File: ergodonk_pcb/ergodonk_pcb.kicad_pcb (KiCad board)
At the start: 2 copper layers, 184 x 152.6 mm, 120 parts, among them J1 AudioJack4, Q1 TIP120, SW1 SW_PUSH-MX_W_LED, SW4 SW_PUSH

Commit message: Button & LED reference sync
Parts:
- removed SW1: SW_PUSH-MX_W_LED, SofleChoc:SK6812MINI_and_cherry
- removed SW4: SW_PUSH, SofleChoc:Choc_Hotswap_SK6812MiniE

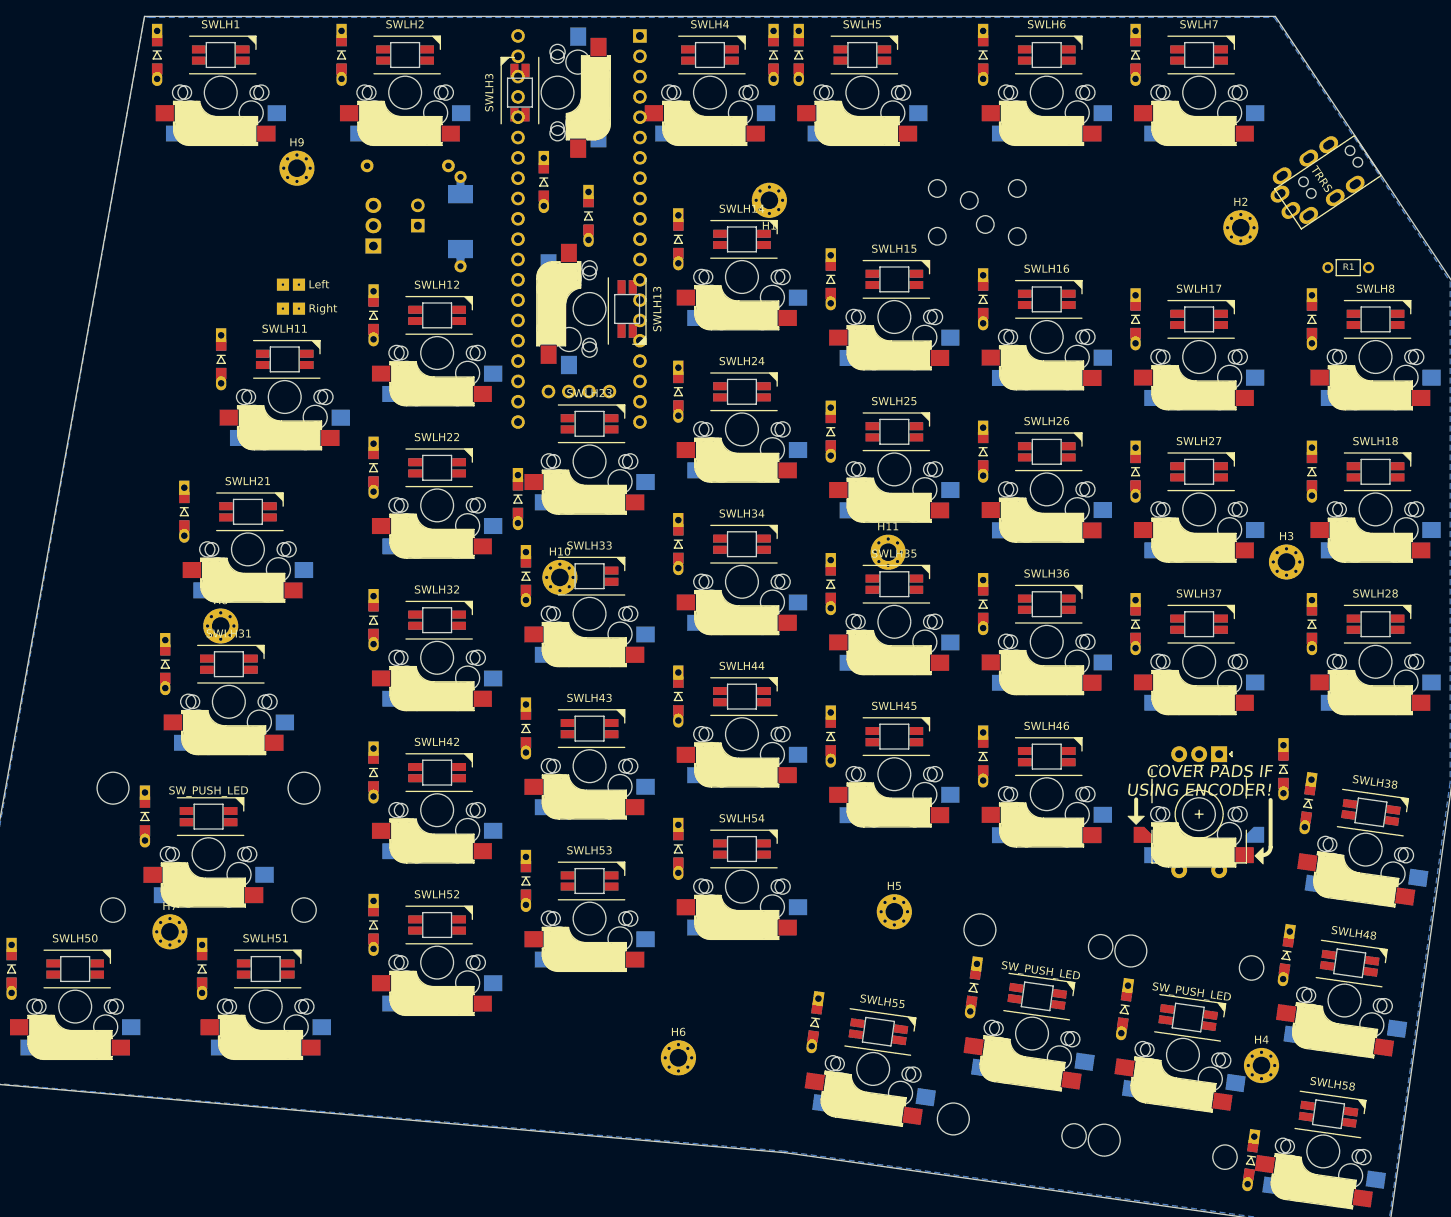
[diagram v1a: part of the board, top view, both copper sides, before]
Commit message: Reveresed nrow/column umbering systme to support double sided
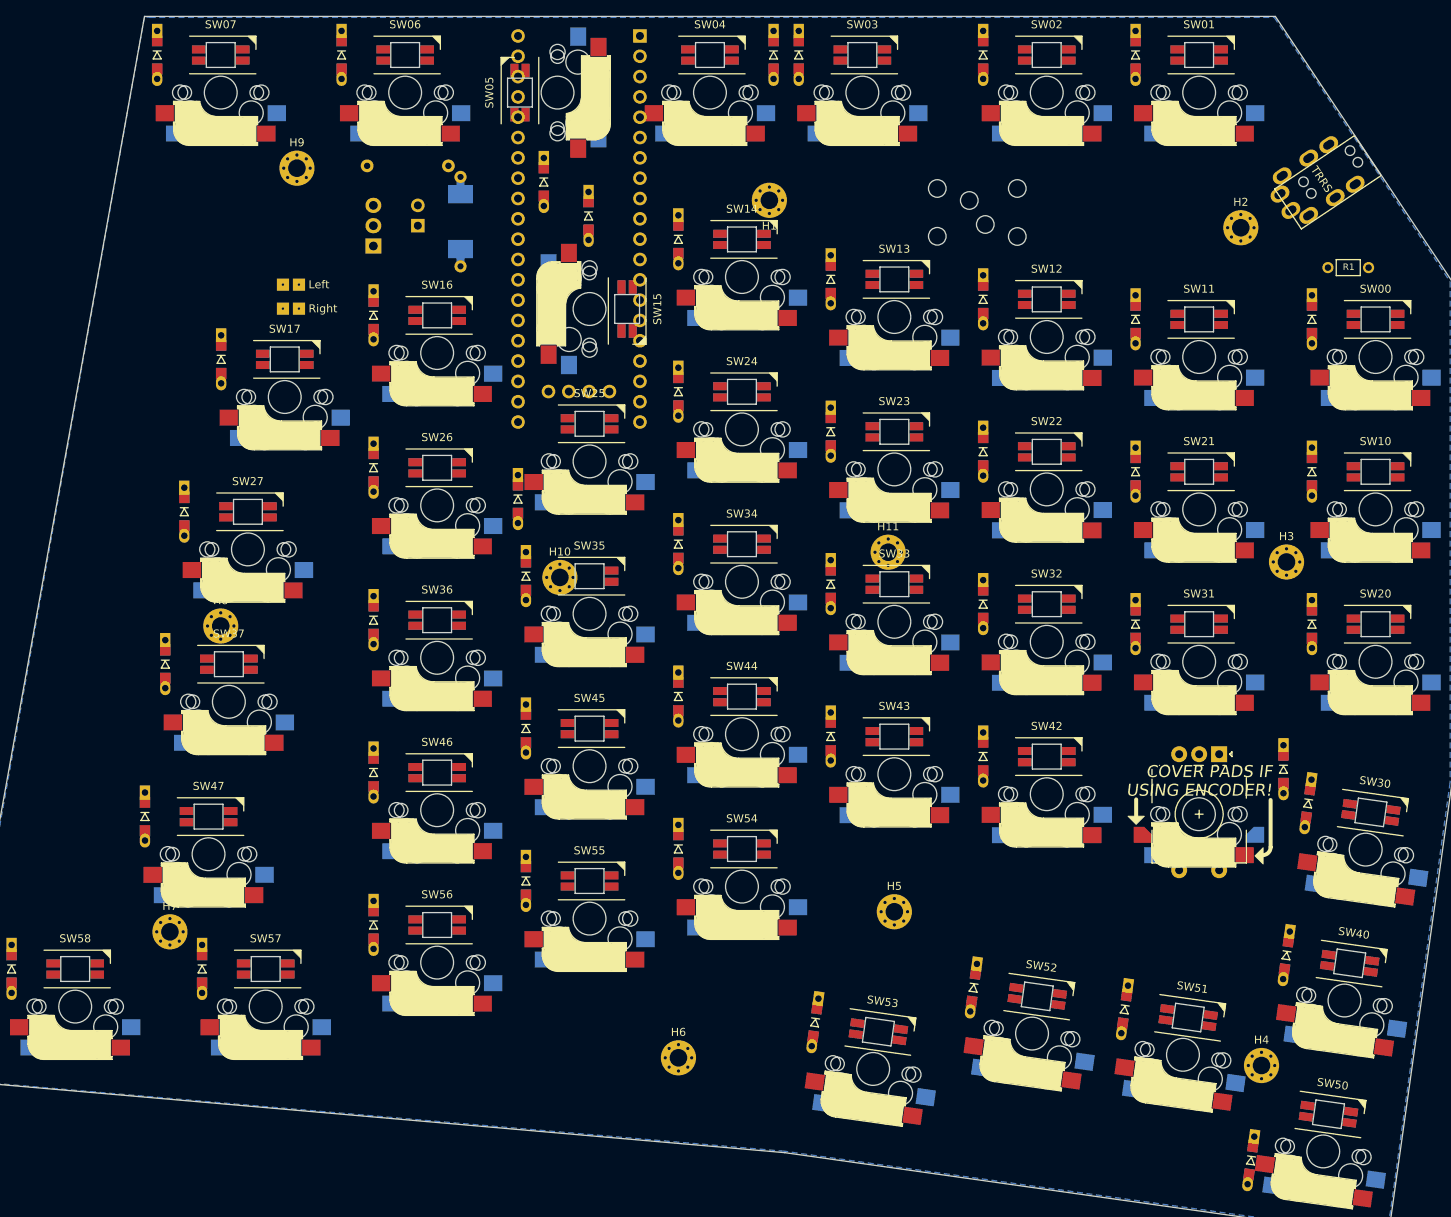
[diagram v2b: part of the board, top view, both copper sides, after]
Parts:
- SW27: renamed from SWLH21; footprint ergodonk_kicad_library:CherryMX_DoubleSided_Hotswap_miniE_1.5u -> ergodonk_kicad_library:CherryMX_DoubleSided_Hotswap_miniE
- SW37: renamed from SWLH31; footprint ergodonk_kicad_library:CherryMX_DoubleSided_Hotswap_miniE_1.75u -> ergodonk_kicad_library:CherryMX_DoubleSided_Hotswap_miniE
- SW47: renamed from SWLH41; footprint ergodonk_kicad_library:CherryMX_DoubleSided_Hotswap_miniE_2u -> ergodonk_kicad_library:CherryMX_DoubleSided_Hotswap_miniE
- SW51: renamed from SWLH57; footprint ergodonk_kicad_library:CherryMX_DoubleSided_Hotswap_miniE_2u_Vertical -> ergodonk_kicad_library:CherryMX_DoubleSided_Hotswap_miniE
- SW52: renamed from SWLH56; footprint ergodonk_kicad_library:CherryMX_DoubleSided_Hotswap_miniE_2u_Vertical -> ergodonk_kicad_library:CherryMX_DoubleSided_Hotswap_miniE
- SW53: renamed from SWLH55; footprint ergodonk_kicad_library:CherryMX_DoubleSided_Hotswap_miniE_1.25u_Vertical -> ergodonk_kicad_library:CherryMX_DoubleSided_Hotswap_miniE
- SW57: renamed from SWLH51; footprint ergodonk_kicad_library:CherryMX_DoubleSided_Hotswap_miniE_1.25u -> ergodonk_kicad_library:CherryMX_DoubleSided_Hotswap_miniE
- SW58: renamed from SWLH50; footprint ergodonk_kicad_library:CherryMX_DoubleSided_Hotswap_miniE_1.25u -> ergodonk_kicad_library:CherryMX_DoubleSided_Hotswap_miniE
- renumbered D8 to D00, D7 to D01, D6 to D02, D5 to D03, D4 to D04, D3 to D05, D2 to D06, D1 to D07, D18 to D10, D17 to D11, D16 to D12, D15 to D13, D13 to D15, D12 to D16, D11 to D17, D28 to D20, D27 to D21, D26 to D22, D25 to D23, D23 to D25, D22 to D26, D21 to D27, D38 to D30, D37 to D31, D36 to D32, D35 to D33, D33 to D35, D32 to D36, D31 to D37, D48 to D40, D47 to D41, D46 to D42, D45 to D43, D43 to D45, D42 to D46, D41 to D47, D58 to D50, D57 to D51, D56 to D52, D55 to D53, D53 to D55, D52 to D56, D51 to D57, D50 to D58, SWLH8 to SW00, SWLH7 to SW01, SWLH6 to SW02, SWLH5 to SW03, SWLH4 to SW04, SWLH3 to SW05, SWLH2 to SW06, SWLH1 to SW07, SWLH18 to SW10, SWLH17 to SW11, SWLH16 to SW12, SWLH15 to SW13, SWLH14 to SW14, SWLH13 to SW15, SWLH12 to SW16, SWLH11 to SW17, SWLH28 to SW20, SWLH27 to SW21, SWLH26 to SW22, SWLH25 to SW23, SWLH24 to SW24, SWLH23 to SW25, SWLH22 to SW26, SWLH38 to SW30, SWLH37 to SW31, SWLH36 to SW32, SWLH35 to SW33, SWLH34 to SW34, SWLH33 to SW35, SWLH32 to SW36, SWLH48 to SW40, SWLH46 to SW42, SWLH45 to SW43, SWLH44 to SW44, SWLH43 to SW45, SWLH42 to SW46, SWLH58 to SW50, SWLH54 to SW54, SWLH53 to SW55, SWLH52 to SW56
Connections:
- net SW47B renamed SW41B
- D00 pad 2: Net-(D8-Pad2) -> Net-(SW00-Pad5)
- D01 pad 2: Net-(D7-Pad2) -> Net-(D01-Pad2)
- D02 pad 2: Net-(D6-Pad2) -> Net-(D02-Pad2)
- D03 pad 2: Net-(D5-Pad2) -> Net-(D03-Pad2)
- D04 pad 2: Net-(D4-Pad2) -> Net-(D04-Pad2)
- D05 pad 2: Net-(D3-Pad2) -> Net-(D05-Pad2)
- D06 pad 2: Net-(D2-Pad2) -> Net-(D06-Pad2)
- D07 pad 2: Net-(D1-Pad2) -> Net-(D07-Pad2)
- D10 pad 2: Net-(D18-Pad2) -> Net-(D10-Pad2)
- D11 pad 2: Net-(D17-Pad2) -> Net-(D11-Pad2)
- D12 pad 2: Net-(D16-Pad2) -> Net-(D12-Pad2)
- D13 pad 2: Net-(D15-Pad2) -> Net-(D13-Pad2)
- D15 pad 2: Net-(D13-Pad2) -> Net-(D15-Pad2)
- D16 pad 2: Net-(D12-Pad2) -> Net-(D16-Pad2)
- D17 pad 2: Net-(D11-Pad2) -> Net-(D17-Pad2)
- D20 pad 2: Net-(D28-Pad2) -> Net-(D20-Pad2)
- D21 pad 2: Net-(D27-Pad2) -> Net-(D21-Pad2)
- D22 pad 2: Net-(D26-Pad2) -> Net-(D22-Pad2)
- D23 pad 2: Net-(D25-Pad2) -> Net-(D23-Pad2)
- D25 pad 2: Net-(D23-Pad2) -> Net-(D25-Pad2)
- D26 pad 2: Net-(D22-Pad2) -> Net-(D26-Pad2)
- D27 pad 2: Net-(D21-Pad2) -> Net-(D27-Pad2)
- D30 pad 2: Net-(D38-Pad2) -> Net-(D30-Pad2)
- D31 pad 2: Net-(D37-Pad2) -> Net-(D31-Pad2)
- D32 pad 2: Net-(D36-Pad2) -> Net-(D32-Pad2)
- D33 pad 2: Net-(D35-Pad2) -> Net-(D33-Pad2)
- D35 pad 2: Net-(D33-Pad2) -> Net-(D35-Pad2)
- D36 pad 2: Net-(D32-Pad2) -> Net-(D36-Pad2)
- D37 pad 2: Net-(D31-Pad2) -> Net-(D37-Pad2)
- D40 pad 2: Net-(D48-Pad2) -> Net-(SW40-Pad5)
- D42 pad 2: Net-(D46-Pad2) -> Net-(SW42-Pad5)
- D43 pad 2: Net-(D45-Pad2) -> Net-(SW43-Pad5)
- D44 pad 2: Net-(D44-Pad2) -> Net-(SW44-Pad5)
- D45 pad 2: Net-(D43-Pad2) -> Net-(SW45-Pad5)
- D46 pad 2: Net-(D42-Pad2) -> Net-(SW46-Pad5)
- D47 pad 2: Net-(D41-Pad2) -> Net-(SW47-Pad5)
- D50 pad 2: Net-(D58-Pad2) -> Net-(D50-Pad2)
- D51 pad 2: Net-(D57-Pad2) -> Net-(D51-Pad2)
- D52 pad 2: Net-(D56-Pad2) -> Net-(D52-Pad2)
- D53 pad 2: Net-(D55-Pad2) -> Net-(D53-Pad2)
- D55 pad 2: Net-(D53-Pad2) -> Net-(D55-Pad2)
- D56 pad 2: Net-(D52-Pad2) -> Net-(D56-Pad2)
- D57 pad 2: Net-(D51-Pad2) -> Net-(D57-Pad2)
- D58 pad 2: Net-(D50-Pad2) -> Net-(D58-Pad2)
- SW00 pad 1: col8 -> VDD
- SW00 pad 2: Net-(D8-Pad2) -> unconnected-(SW00-Pad2)
- SW00 pad 3: (no net) -> GND
- SW00 pad 4: (no net) -> unconnected-(SW00-Pad4)
- SW00 pad 5: (no net) -> Net-(SW00-Pad5)
- SW00 pad 6: (no net) -> col8
- SW01 pad 1: SW47A -> VDD
- SW01 pad 2: Net-(D7-Pad2) -> unconnected-(SW01-Pad2)
- SW01 pad 3: (no net) -> GND
- SW01 pad 4: (no net) -> unconnected-(SW01-Pad4)
- SW01 pad 5: (no net) -> Net-(D01-Pad2)
- SW01 pad 6: (no net) -> SW41A
- SW02 pad 1: col6 -> VDD
- SW02 pad 2: Net-(D6-Pad2) -> unconnected-(SW02-Pad2)
- SW02 pad 3: (no net) -> GND
- SW02 pad 4: (no net) -> unconnected-(SW02-Pad4)
- SW02 pad 5: (no net) -> Net-(D02-Pad2)
- SW02 pad 6: (no net) -> col2
- SW03 pad 1: col5 -> VDD
- SW03 pad 2: Net-(D5-Pad2) -> unconnected-(SW03-Pad2)
- SW03 pad 3: (no net) -> GND
- SW03 pad 4: (no net) -> unconnected-(SW03-Pad4)
- SW03 pad 5: (no net) -> Net-(D03-Pad2)
- SW03 pad 6: (no net) -> col3
- SW04 pad 1: col4 -> VDD
- SW04 pad 2: Net-(D4-Pad2) -> unconnected-(SW04-Pad2)
- SW04 pad 3: (no net) -> GND
- SW04 pad 4: (no net) -> unconnected-(SW04-Pad4)
- SW04 pad 5: (no net) -> Net-(D04-Pad2)
- SW04 pad 6: (no net) -> col4
- SW05 pad 1: col3 -> VDD
- SW05 pad 2: Net-(D3-Pad2) -> unconnected-(SW05-Pad2)
- SW05 pad 3: (no net) -> GND
- SW05 pad 4: (no net) -> unconnected-(SW05-Pad4)
- SW05 pad 5: (no net) -> Net-(D05-Pad2)
- SW05 pad 6: (no net) -> col5
- SW06 pad 1: col2 -> VDD
- SW06 pad 2: Net-(D2-Pad2) -> unconnected-(SW06-Pad2)
- SW06 pad 3: (no net) -> GND
- SW06 pad 4: (no net) -> unconnected-(SW06-Pad4)
- SW06 pad 5: (no net) -> Net-(D06-Pad2)
- SW06 pad 6: (no net) -> col6
- SW07 pad 1: col1 -> VDD
- SW07 pad 2: Net-(D1-Pad2) -> unconnected-(SW07-Pad2)
- SW07 pad 3: (no net) -> GND
- SW07 pad 4: (no net) -> unconnected-(SW07-Pad4)
- SW07 pad 5: (no net) -> Net-(D07-Pad2)
- SW07 pad 6: (no net) -> SW41A
- SW10 pad 1: col8 -> VDD
- SW10 pad 2: Net-(D18-Pad2) -> unconnected-(SW10-Pad2)
- SW10 pad 3: (no net) -> GND
- SW10 pad 4: (no net) -> unconnected-(SW10-Pad4)
- SW10 pad 5: (no net) -> Net-(D10-Pad2)
- SW10 pad 6: (no net) -> col8
- SW11 pad 1: SW47A -> VDD
- SW11 pad 2: Net-(D17-Pad2) -> Net-(SW11-Pad2)
- SW11 pad 3: (no net) -> GND
- SW11 pad 4: (no net) -> LED
- SW11 pad 5: (no net) -> Net-(D11-Pad2)
- SW11 pad 6: (no net) -> SW41A
- SW12 pad 1: col6 -> VDD
- SW12 pad 2: Net-(D16-Pad2) -> Net-(SW12-Pad2)
- SW12 pad 3: (no net) -> GND
- SW12 pad 4: (no net) -> Net-(SW11-Pad2)
- SW12 pad 5: (no net) -> Net-(D12-Pad2)
- SW12 pad 6: (no net) -> col2
- SW13 pad 1: col5 -> VDD
- SW13 pad 2: Net-(D15-Pad2) -> Net-(SW13-Pad2)
- SW13 pad 3: (no net) -> GND
- SW13 pad 4: (no net) -> Net-(SW12-Pad2)
- SW13 pad 5: (no net) -> Net-(D13-Pad2)
- SW13 pad 6: (no net) -> col3
- SW14 pad 1: col4 -> VDD
- SW14 pad 2: Net-(D14-Pad2) -> Net-(SW14-Pad2)
- SW14 pad 3: (no net) -> GND
- SW14 pad 4: (no net) -> Net-(SW13-Pad2)
- SW14 pad 5: (no net) -> Net-(D14-Pad2)
- SW14 pad 6: (no net) -> col4
- SW15 pad 1: col3 -> VDD
- SW15 pad 2: Net-(D13-Pad2) -> Net-(SW15-Pad2)
- SW15 pad 3: (no net) -> GND
- SW15 pad 4: (no net) -> Net-(SW14-Pad2)
- SW15 pad 5: (no net) -> Net-(D15-Pad2)
- SW15 pad 6: (no net) -> col5
- SW16 pad 1: col2 -> VDD
- SW16 pad 2: Net-(D12-Pad2) -> Net-(SW16-Pad2)
- SW16 pad 3: (no net) -> GND
- SW16 pad 4: (no net) -> Net-(SW15-Pad2)
- SW16 pad 5: (no net) -> Net-(D16-Pad2)
- SW16 pad 6: (no net) -> col6
- SW17 pad 1: col1 -> VDD
- SW17 pad 2: Net-(D11-Pad2) -> Net-(SW17-Pad2)
- SW17 pad 3: (no net) -> GND
- SW17 pad 4: (no net) -> Net-(SW16-Pad2)
- SW17 pad 5: (no net) -> Net-(D17-Pad2)
- SW17 pad 6: (no net) -> SW41A
- SW20 pad 1: col8 -> VDD
- SW20 pad 2: Net-(D28-Pad2) -> unconnected-(SW20-Pad2)
- SW20 pad 3: (no net) -> GND
- SW20 pad 4: (no net) -> unconnected-(SW20-Pad4)
- SW20 pad 5: (no net) -> Net-(D20-Pad2)
- SW20 pad 6: (no net) -> col8
- SW21 pad 1: SW47A -> VDD
- SW21 pad 2: Net-(D27-Pad2) -> Net-(SW21-Pad2)
- SW21 pad 3: (no net) -> GND
- SW21 pad 4: (no net) -> Net-(SW21-Pad4)
- SW21 pad 5: (no net) -> Net-(D21-Pad2)
- SW21 pad 6: (no net) -> SW41A
- SW22 pad 1: col6 -> VDD
- SW22 pad 2: Net-(D26-Pad2) -> Net-(SW21-Pad4)
- SW22 pad 3: (no net) -> GND
- SW22 pad 4: (no net) -> Net-(SW22-Pad4)
- SW22 pad 5: (no net) -> Net-(D22-Pad2)
- SW22 pad 6: (no net) -> col2
- SW23 pad 1: col5 -> VDD
- SW23 pad 2: Net-(D25-Pad2) -> Net-(SW22-Pad4)
- SW23 pad 3: (no net) -> GND
- SW23 pad 4: (no net) -> Net-(SW23-Pad4)
- SW23 pad 5: (no net) -> Net-(D23-Pad2)
- SW23 pad 6: (no net) -> col3
- SW24 pad 1: col4 -> VDD
- SW24 pad 2: Net-(D24-Pad2) -> Net-(SW23-Pad4)
- SW24 pad 3: (no net) -> GND
- SW24 pad 4: (no net) -> Net-(SW24-Pad4)
- SW24 pad 5: (no net) -> Net-(D24-Pad2)
- SW24 pad 6: (no net) -> col4
- SW25 pad 1: col3 -> VDD
- SW25 pad 2: Net-(D23-Pad2) -> Net-(SW24-Pad4)
- SW25 pad 3: (no net) -> GND
- SW25 pad 4: (no net) -> Net-(SW25-Pad4)
- SW25 pad 5: (no net) -> Net-(D25-Pad2)
- SW25 pad 6: (no net) -> col5
- SW26 pad 1: col2 -> VDD
- SW26 pad 2: Net-(D22-Pad2) -> Net-(SW25-Pad4)
- SW26 pad 3: (no net) -> GND
- SW26 pad 4: (no net) -> Net-(SW26-Pad4)
- SW26 pad 5: (no net) -> Net-(D26-Pad2)
- SW26 pad 6: (no net) -> col6
- SW27 pad 1: col1 -> VDD
- SW27 pad 2: Net-(D21-Pad2) -> Net-(SW26-Pad4)
- SW27 pad 3: (no net) -> GND
- SW27 pad 4: (no net) -> Net-(SW17-Pad2)
- SW27 pad 5: (no net) -> Net-(D27-Pad2)
- SW27 pad 6: (no net) -> SW41A
- SW30 pad 1: col8 -> VDD
- SW30 pad 2: Net-(D38-Pad2) -> unconnected-(SW30-Pad2)
- SW30 pad 3: (no net) -> GND
- SW30 pad 4: (no net) -> unconnected-(SW30-Pad4)
- SW30 pad 5: (no net) -> Net-(D30-Pad2)
- SW30 pad 6: (no net) -> col8
- SW31 pad 1: SW47A -> VDD
- SW31 pad 2: Net-(D37-Pad2) -> Net-(SW31-Pad2)
- SW31 pad 3: (no net) -> GND
- SW31 pad 4: (no net) -> Net-(SW21-Pad2)
- SW31 pad 5: (no net) -> Net-(D31-Pad2)
- SW31 pad 6: (no net) -> SW41A
- SW32 pad 1: col6 -> VDD
- SW32 pad 2: Net-(D36-Pad2) -> Net-(SW32-Pad2)
- SW32 pad 3: (no net) -> GND
- SW32 pad 4: (no net) -> Net-(SW31-Pad2)
- SW32 pad 5: (no net) -> Net-(D32-Pad2)
- SW32 pad 6: (no net) -> col2
- SW33 pad 1: col5 -> VDD
- SW33 pad 2: Net-(D35-Pad2) -> Net-(SW33-Pad2)
- SW33 pad 3: (no net) -> GND
- SW33 pad 4: (no net) -> Net-(SW32-Pad2)
- SW33 pad 5: (no net) -> Net-(D33-Pad2)
- SW33 pad 6: (no net) -> col3
- SW34 pad 1: col4 -> VDD
- SW34 pad 2: Net-(D34-Pad2) -> Net-(SW34-Pad2)
- SW34 pad 3: (no net) -> GND
- SW34 pad 4: (no net) -> Net-(SW33-Pad2)
- SW34 pad 5: (no net) -> Net-(D34-Pad2)
- SW34 pad 6: (no net) -> col4
- SW35 pad 1: col3 -> VDD
- SW35 pad 2: Net-(D33-Pad2) -> Net-(SW35-Pad2)
- SW35 pad 3: (no net) -> GND
- SW35 pad 4: (no net) -> Net-(SW34-Pad2)
- SW35 pad 5: (no net) -> Net-(D35-Pad2)
- SW35 pad 6: (no net) -> col5
- SW36 pad 1: col2 -> VDD
- SW36 pad 2: Net-(D32-Pad2) -> Net-(SW36-Pad2)
- SW36 pad 3: (no net) -> GND
- SW36 pad 4: (no net) -> Net-(SW35-Pad2)
- SW36 pad 5: (no net) -> Net-(D36-Pad2)
- SW36 pad 6: (no net) -> col6
- SW37 pad 1: col1 -> VDD
- SW37 pad 2: Net-(D31-Pad2) -> Net-(SW37-Pad2)
- SW37 pad 3: (no net) -> GND
- SW37 pad 4: (no net) -> Net-(SW36-Pad2)
- SW37 pad 5: (no net) -> Net-(D37-Pad2)
- SW37 pad 6: (no net) -> SW41A
- SW40 pad 1: col8 -> VDD
- SW40 pad 2: Net-(D48-Pad2) -> unconnected-(SW40-Pad2)
- SW40 pad 3: (no net) -> GND
- SW40 pad 4: (no net) -> unconnected-(SW40-Pad4)
- SW40 pad 5: (no net) -> Net-(SW40-Pad5)
- SW40 pad 6: (no net) -> col8
- SW42 pad 1: col6 -> VDD
- SW42 pad 2: Net-(D46-Pad2) -> Net-(SW42-Pad2)
- SW42 pad 3: (no net) -> GND
- SW42 pad 4: (no net) -> Net-(SW42-Pad4)
- SW42 pad 5: (no net) -> Net-(SW42-Pad5)
- SW42 pad 6: (no net) -> col2
- SW43 pad 1: col5 -> VDD
- SW43 pad 2: Net-(D45-Pad2) -> Net-(SW42-Pad4)
- SW43 pad 3: (no net) -> GND
- SW43 pad 4: (no net) -> Net-(SW43-Pad4)
- SW43 pad 5: (no net) -> Net-(SW43-Pad5)
- SW43 pad 6: (no net) -> col3
- SW44 pad 1: col4 -> VDD
- SW44 pad 2: Net-(D44-Pad2) -> Net-(SW43-Pad4)
- SW44 pad 3: (no net) -> GND
- SW44 pad 4: (no net) -> Net-(SW44-Pad4)
- SW44 pad 5: (no net) -> Net-(SW44-Pad5)
- SW44 pad 6: (no net) -> col4
- SW45 pad 1: col3 -> VDD
- SW45 pad 2: Net-(D43-Pad2) -> Net-(SW44-Pad4)
- SW45 pad 3: (no net) -> GND
- SW45 pad 4: (no net) -> Net-(SW45-Pad4)
- SW45 pad 5: (no net) -> Net-(SW45-Pad5)
- SW45 pad 6: (no net) -> col5
- SW46 pad 1: col2 -> VDD
- SW46 pad 2: Net-(D42-Pad2) -> Net-(SW45-Pad4)
- SW46 pad 3: (no net) -> GND
- SW46 pad 4: (no net) -> Net-(SW46-Pad4)
- SW46 pad 5: (no net) -> Net-(SW46-Pad5)
- SW46 pad 6: (no net) -> col6
- SW47 pad 1: col1 -> VDD
- SW47 pad 2: Net-(D41-Pad2) -> Net-(SW46-Pad4)
- SW47 pad 3: (no net) -> GND
- SW47 pad 4: (no net) -> Net-(SW37-Pad2)
- SW47 pad 5: (no net) -> Net-(SW47-Pad5)
- SW47 pad 6: (no net) -> SW41A
- SW50 pad 1: col8 -> VDD
- SW50 pad 2: Net-(D58-Pad2) -> unconnected-(SW50-Pad2)
- SW50 pad 3: (no net) -> GND
- SW50 pad 4: (no net) -> unconnected-(SW50-Pad4)
- SW50 pad 5: (no net) -> Net-(D50-Pad2)
- SW50 pad 6: (no net) -> col8
- SW51 pad 1: SW47A -> VDD
- SW51 pad 2: Net-(D57-Pad2) -> unconnected-(SW51-Pad2)
- SW51 pad 3: (no net) -> GND
- SW51 pad 4: (no net) -> unconnected-(SW51-Pad4)
- SW51 pad 5: (no net) -> Net-(D51-Pad2)
- SW51 pad 6: (no net) -> SW41A
- SW52 pad 1: col6 -> VDD
- SW52 pad 2: Net-(D56-Pad2) -> unconnected-(SW52-Pad2)
- SW52 pad 3: (no net) -> GND
- SW52 pad 4: (no net) -> unconnected-(SW52-Pad4)
- SW52 pad 5: (no net) -> Net-(D52-Pad2)
- SW52 pad 6: (no net) -> col2
- SW53 pad 1: col5 -> VDD
- SW53 pad 2: Net-(D55-Pad2) -> unconnected-(SW53-Pad2)
- SW53 pad 3: (no net) -> GND
- SW53 pad 4: (no net) -> unconnected-(SW53-Pad4)
- SW53 pad 5: (no net) -> Net-(D53-Pad2)
- SW53 pad 6: (no net) -> col3
- SW54 pad 1: col4 -> VDD
- SW54 pad 2: Net-(D54-Pad2) -> Net-(SW54-Pad2)
- SW54 pad 3: (no net) -> GND
- SW54 pad 4: (no net) -> Net-(SW42-Pad2)
- SW54 pad 5: (no net) -> Net-(D54-Pad2)
- SW54 pad 6: (no net) -> col4
- SW55 pad 1: col3 -> VDD
- SW55 pad 2: Net-(D53-Pad2) -> Net-(SW55-Pad2)
- SW55 pad 3: (no net) -> GND
- SW55 pad 4: (no net) -> Net-(SW54-Pad2)
- SW55 pad 5: (no net) -> Net-(D55-Pad2)
- SW55 pad 6: (no net) -> col5
- SW56 pad 1: col2 -> VDD
- SW56 pad 2: Net-(D52-Pad2) -> Net-(SW56-Pad2)
- SW56 pad 3: (no net) -> GND
- SW56 pad 4: (no net) -> Net-(SW55-Pad2)
- SW56 pad 5: (no net) -> Net-(D56-Pad2)
- SW56 pad 6: (no net) -> col6
- SW57 pad 1: col1 -> VDD
- SW57 pad 2: Net-(D51-Pad2) -> Net-(SW57-Pad2)
- SW57 pad 3: (no net) -> GND
- SW57 pad 4: (no net) -> Net-(SW56-Pad2)
- SW57 pad 5: (no net) -> Net-(D57-Pad2)
- SW57 pad 6: (no net) -> SW41A
- SW58 pad 1: col0 -> VDD
- SW58 pad 2: Net-(D50-Pad2) -> unconnected-(SW58-Pad2)
- SW58 pad 3: (no net) -> GND
- SW58 pad 4: (no net) -> Net-(SW57-Pad2)
- SW58 pad 5: (no net) -> Net-(D58-Pad2)
- SW58 pad 6: (no net) -> col8
- SWLH_ROT1 pad S1: SW47A -> SW41A
- ULH1 pad 11: unconnected-(ULH1-Pad11) -> LED
- ULH1 pad 15: SW47A -> SW41A
- ULH1 pad 22: col0 -> col8
- ULH1 pad 23: col1 -> SW41A
